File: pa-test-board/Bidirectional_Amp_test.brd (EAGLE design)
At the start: 30 x 44 mm, 34 parts, among them J1 142-0701-851, J2 142-0701-851, J3 142-0701-851, J4 142-0701-851, SW1 TL36PO, U10 TQP9111

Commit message: Attribues added to parts and BOMs created via ULP
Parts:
- L3: value 1.2nH -> 1.0nH

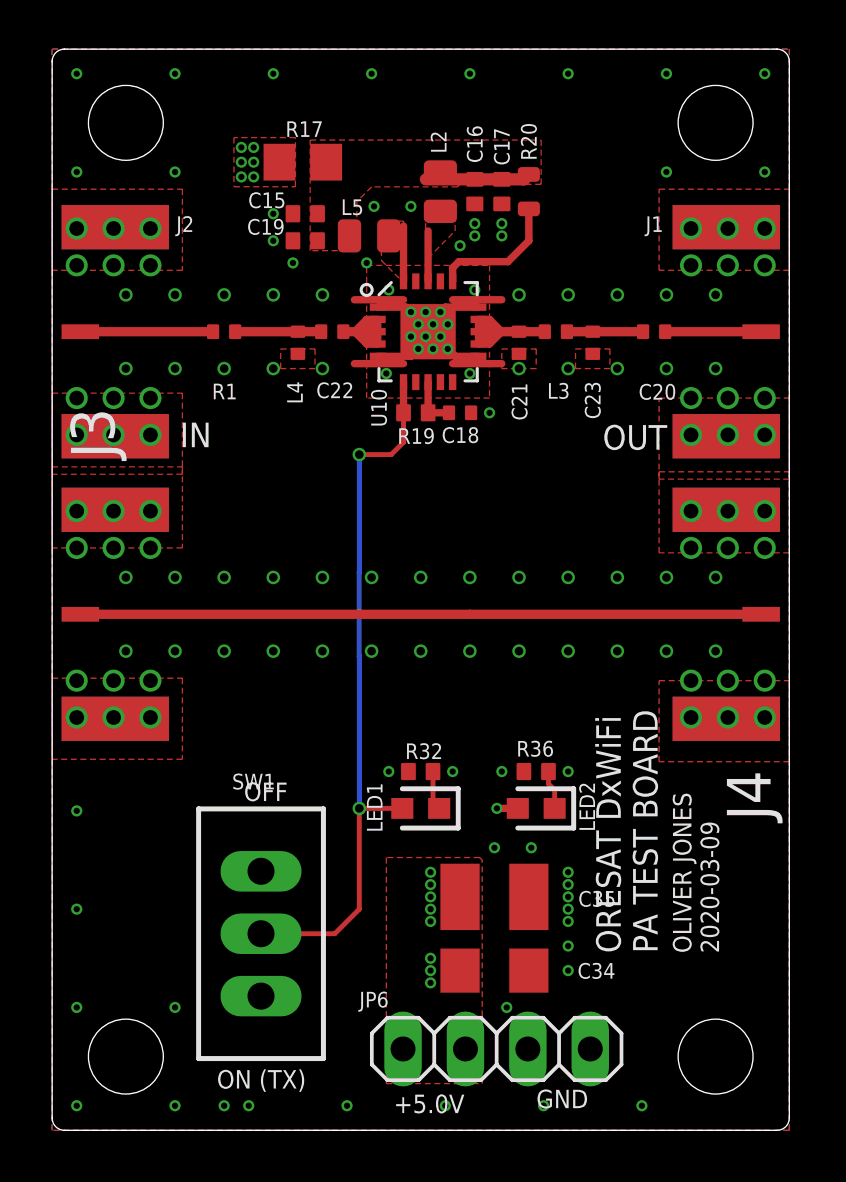
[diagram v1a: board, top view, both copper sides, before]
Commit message: Cleaned up DRCs and stiching.
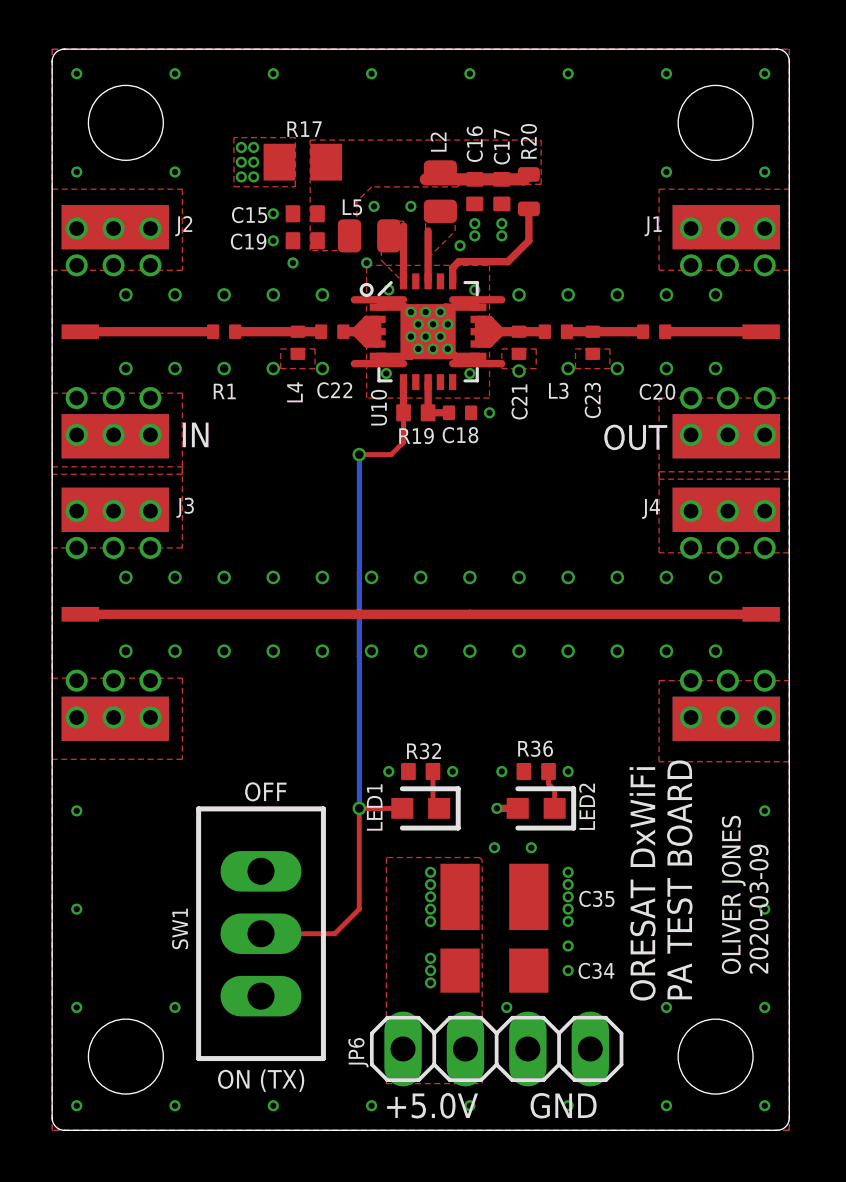
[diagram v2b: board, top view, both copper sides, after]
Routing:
- net N$56: track 7.41 -> 7.93 mm
- net GND: vias 160 -> 164
